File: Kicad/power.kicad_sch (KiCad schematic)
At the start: 25 parts, among them J7 22112042

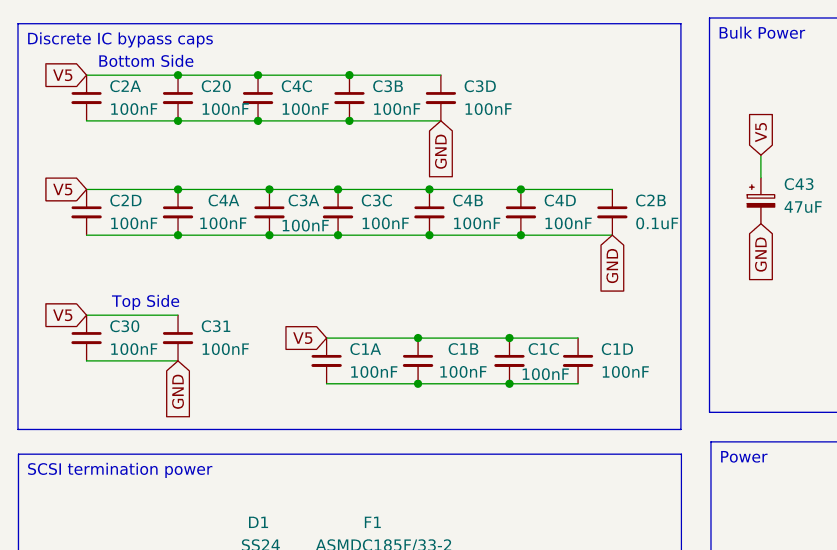
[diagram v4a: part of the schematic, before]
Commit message: Revert: Rename majority of bypass capacitors to match their Uxx
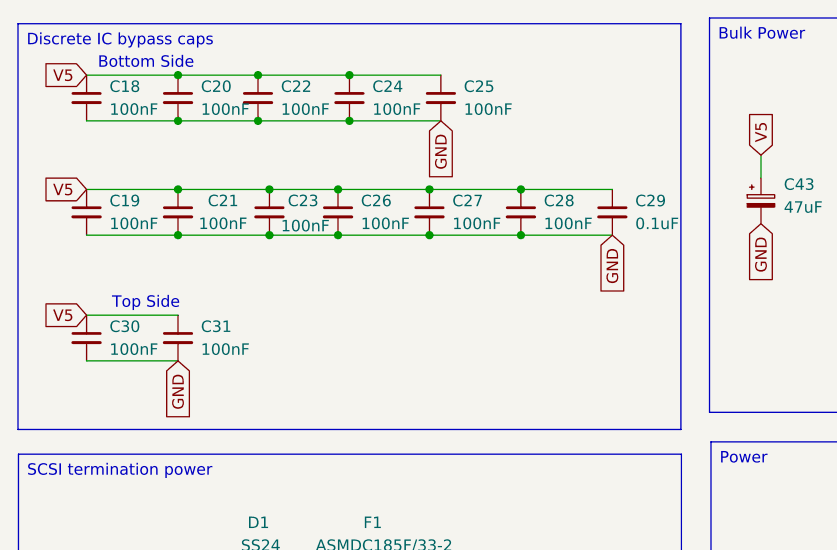
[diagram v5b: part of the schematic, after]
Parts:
- removed C1A, C1B, C1C, C1D: 100nF, Capacitor_SMD:C_0603_1608Metric_Pad1.08x0.95mm_HandSolder, symbol Device:C_Small
- renumbered C2A to C18, C2D to C19, C4A to C21, C4C to C22, C3A to C23, C3B to C24, C3D to C25, C3C to C26, C4B to C27, C4D to C28, C2B to C29

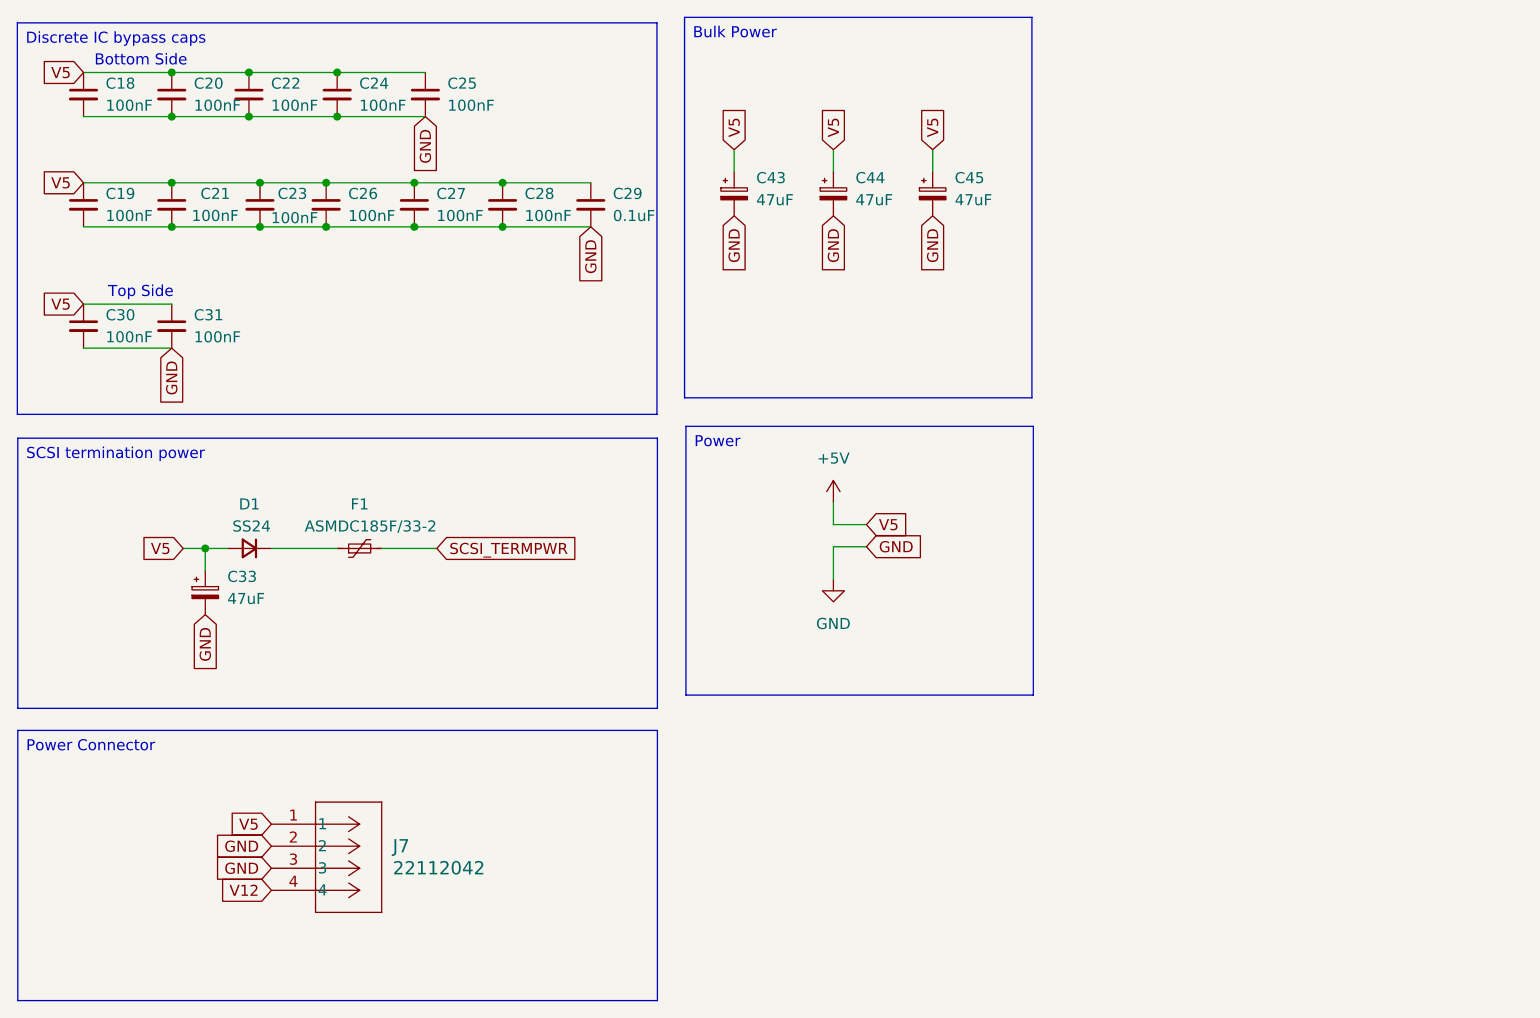
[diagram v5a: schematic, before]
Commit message: Add more bypass caps
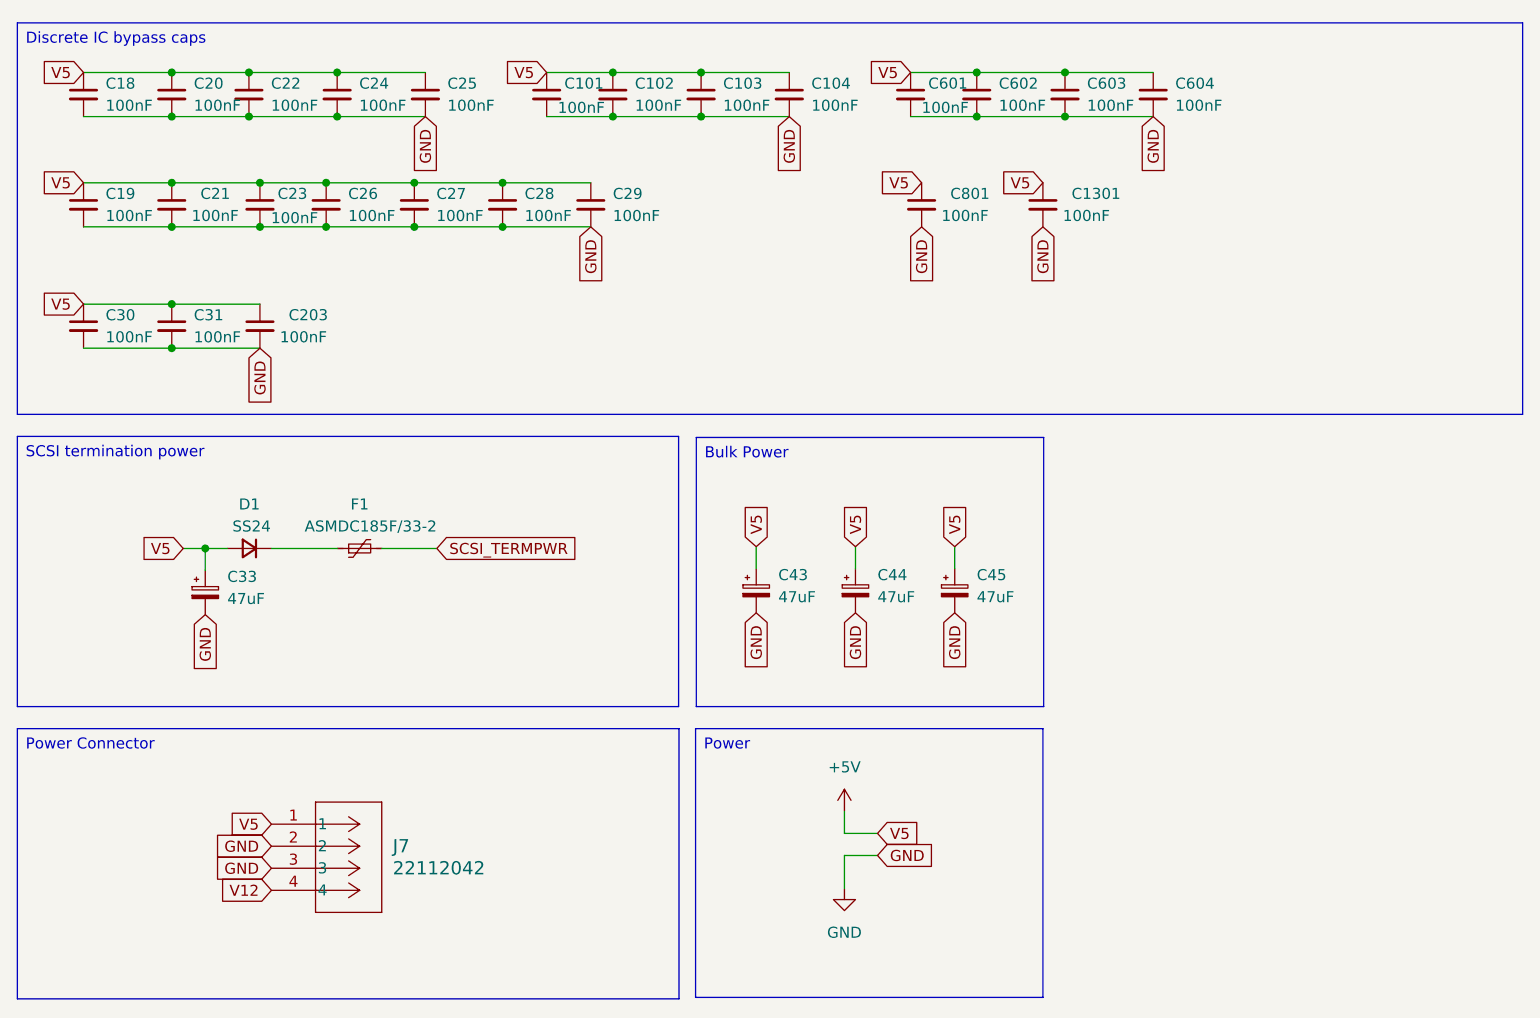
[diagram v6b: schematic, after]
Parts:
- added C101, C102, C103, C104, C1301, C203, C601, C602, C603, C604, C801: 100nF, Capacitor_SMD:C_0603_1608Metric_Pad1.08x0.95mm_HandSolder, symbol Device:C_Small
- C29: value 0.1uF -> 100nF
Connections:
- net +5V: now also C101.1, C102.1, C103.1, C104.1, C1301.1, C203.1, C601.1, C602.1, C603.1, C604.1, C801.1
- net GND: now also C101.2, C102.2, C103.2, C104.2, C1301.2, C203.2, C601.2, C602.2, C603.2, C604.2, C801.2
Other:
- note removed: "Bottom Side"
- note removed: "Top Side"
- moved on the sheet: C43, C44, C45

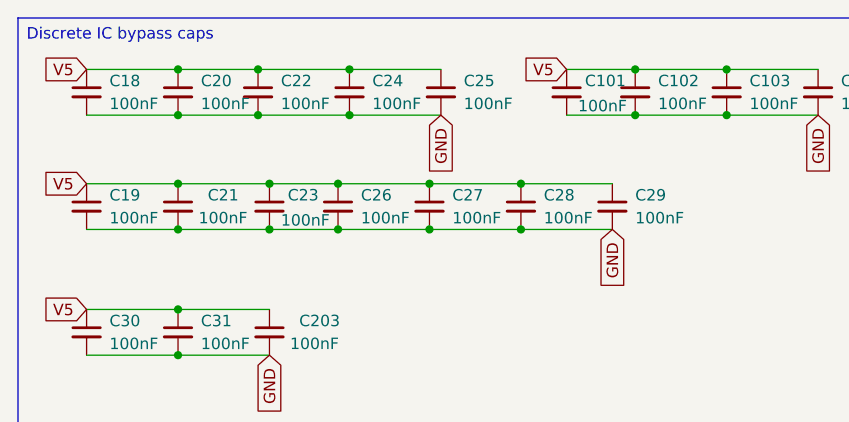
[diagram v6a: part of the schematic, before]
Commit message: Rename capacitors
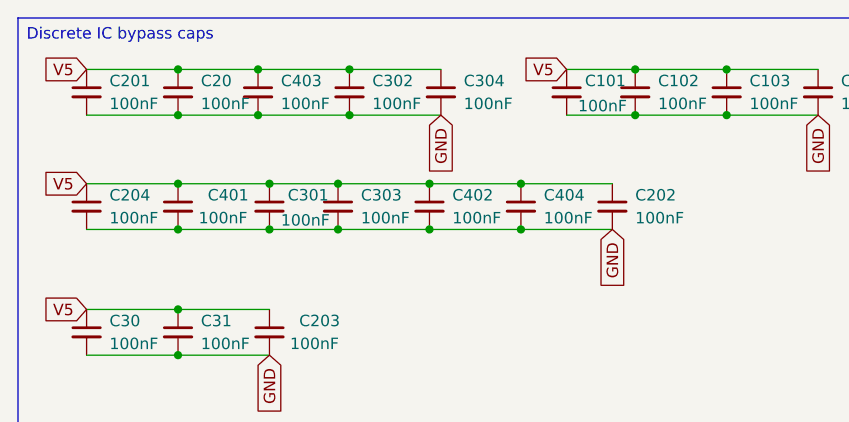
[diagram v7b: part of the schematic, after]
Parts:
- renumbered C18 to C201, C29 to C202, C19 to C204, C23 to C301, C24 to C302, C26 to C303, C25 to C304, C21 to C401, C27 to C402, C22 to C403, C28 to C404
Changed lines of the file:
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@@
 		(on_board yes)
 		(dnp no)
-		(property "Reference" "C23"
+		(property "Reference" "C301"
 			(at 51.562 40.64 0)
 			(effects
@@
 			(project "A4092"
 				(path "/8f9f4021-47aa-41d9-bea7-f6ccf72098bb/166c366c-e5f9-4398-87d9-75fc4b57be99"
-					(reference "C23")
+					(reference "C301")
 					(unit 1)
 				)
@@
 		(dnp no)
 		(fields_autoplaced yes)
-		(property "Reference" "C26"
+		(property "Reference" "C303"
 			(at 59.69 40.6462 0)
 			(effects
@@
 			(project "A4092"
 				(path "/8f9f4021-47aa-41d9-bea7-f6ccf72098bb/166c366c-e5f9-4398-87d9-75fc4b57be99"
-					(reference "C26")
+					(reference "C303")
 					(unit 1)
 				)
@@
 		(dnp no)
 		(fields_autoplaced yes)
-		(property "Reference" "C27"
+		(property "Reference" "C402"
 			(at 69.85 40.6462 0)
 			(effects
@@
 			(project "A4092"
 				(path "/8f9f4021-47aa-41d9-bea7-f6ccf72098bb/166c366c-e5f9-4398-87d9-75fc4b57be99"
-					(reference "C27")
+					(reference "C402")
 					(unit 1)
 				)
@@
 		(dnp no)
 		(fields_autoplaced yes)
-		(property "Reference" "C18"
+		(property "Reference" "C201"
 			(at 31.75 27.9462 0)
 			(effects
@@
 			(project "A4092"
 				(path "/8f9f4021-47aa-41d9-bea7-f6ccf72098bb/166c366c-e5f9-4398-87d9-75fc4b57be99"
-					(reference "C18")
+					(reference "C201")
 					(unit 1)
 				)
@@
 		(on_board yes)
 		(dnp no)
-		(property "Reference" "C21"
+		(property "Reference" "C401"
 			(at 42.672 40.64 0)
 			(effects
@@
 			(project "A4092"
 				(path "/8f9f4021-47aa-41d9-bea7-f6ccf72098bb/166c366c-e5f9-4398-87d9-75fc4b57be99"
-					(reference "C21")
+					(reference "C401")
 					(unit 1)
 				)
@@
 		(dnp no)
 		(fields_autoplaced yes)
-		(property "Reference" "C24"
+		(property "Reference" "C302"
 			(at 60.96 27.9462 0)
 			(effects
@@
 			(project "A4092"
 				(path "/8f9f4021-47aa-41d9-bea7-f6ccf72098bb/166c366c-e5f9-4398-87d9-75fc4b57be99"
-					(reference "C24")
+					(reference "C302")
 					(unit 1)
 				)
@@
 		(dnp no)
 		(fields_autoplaced yes)
-		(property "Reference" "C29"
+		(property "Reference" "C202"
 			(at 90.17 40.6462 0)
 			(effects
@@
 			(project "A4092"
 				(path "/8f9f4021-47aa-41d9-bea7-f6ccf72098bb/166c366c-e5f9-4398-87d9-75fc4b57be99"
-					(reference "C29")
+					(reference "C202")
 					(unit 1)
 				)
@@
 		(dnp no)
 		(fields_autoplaced yes)
-		(property "Reference" "C25"
+		(property "Reference" "C304"
 			(at 71.12 27.9462 0)
 			(effects
@@
 			(project "A4092"
 				(path "/8f9f4021-47aa-41d9-bea7-f6ccf72098bb/166c366c-e5f9-4398-87d9-75fc4b57be99"
-					(reference "C25")
+					(reference "C304")
 					(unit 1)
 				)
@@
 		(dnp no)
 		(fields_autoplaced yes)
-		(property "Reference" "C19"
+		(property "Reference" "C204"
 			(at 31.75 40.6462 0)
 			(effects
@@
 			(project "A4092"
 				(path "/8f9f4021-47aa-41d9-bea7-f6ccf72098bb/166c366c-e5f9-4398-87d9-75fc4b57be99"
-					(reference "C19")
+					(reference "C204")
 					(unit 1)
 				)
@@
 		(dnp no)
 		(fields_autoplaced yes)
-		(property "Reference" "C28"
+		(property "Reference" "C404"
 			(at 80.01 40.6462 0)
 			(effects
@@
 			(project "A4092"
 				(path "/8f9f4021-47aa-41d9-bea7-f6ccf72098bb/166c366c-e5f9-4398-87d9-75fc4b57be99"
-					(reference "C28")
+					(reference "C404")
 					(unit 1)
 				)
@@
 		(dnp no)
 		(fields_autoplaced yes)
-		(property "Reference" "C22"
+		(property "Reference" "C403"
 			(at 50.8 27.9462 0)
 			(effects
@@
 			(project "A4092"
 				(path "/8f9f4021-47aa-41d9-bea7-f6ccf72098bb/166c366c-e5f9-4398-87d9-75fc4b57be99"
-					(reference "C22")
-					(unit 1)
-				)
+					(reference "C403")
+					(unit 1)
+				)

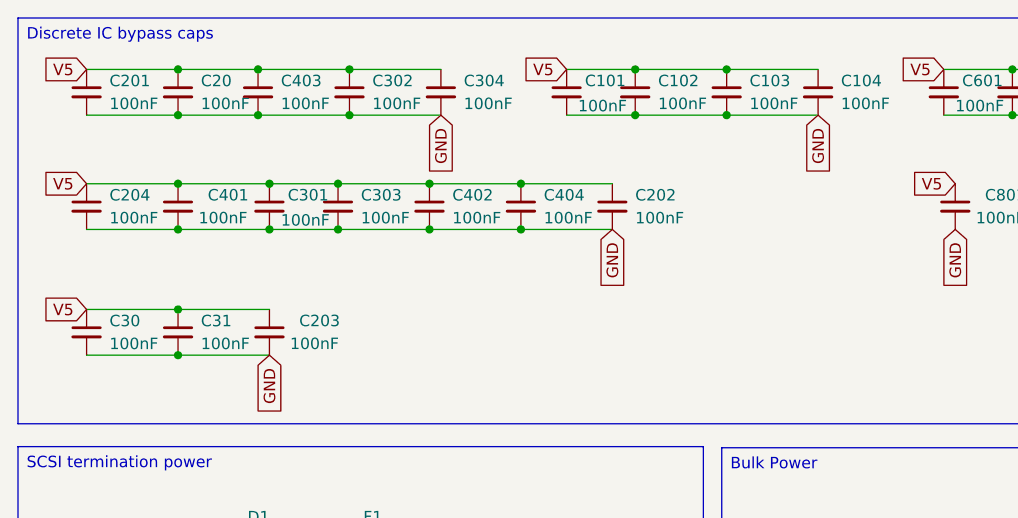
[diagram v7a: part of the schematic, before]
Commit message: Update termination capacitors to tantalum
and clean up bypass caps in schematic
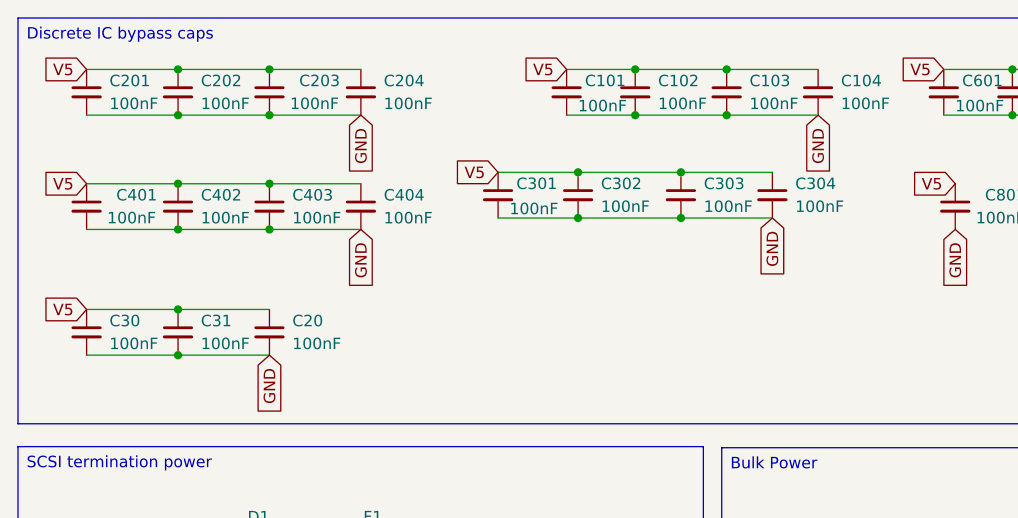
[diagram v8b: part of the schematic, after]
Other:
- moved on the sheet: C20, C202, C203, C204, C301, C302, C303, C304, C401, C402, C403, C404
